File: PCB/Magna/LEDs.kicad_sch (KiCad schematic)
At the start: 94 parts, among them U2001 74HC595, U2002 74HC595, U2003 74HC595, U2004 74HC595, U2005 74HC595

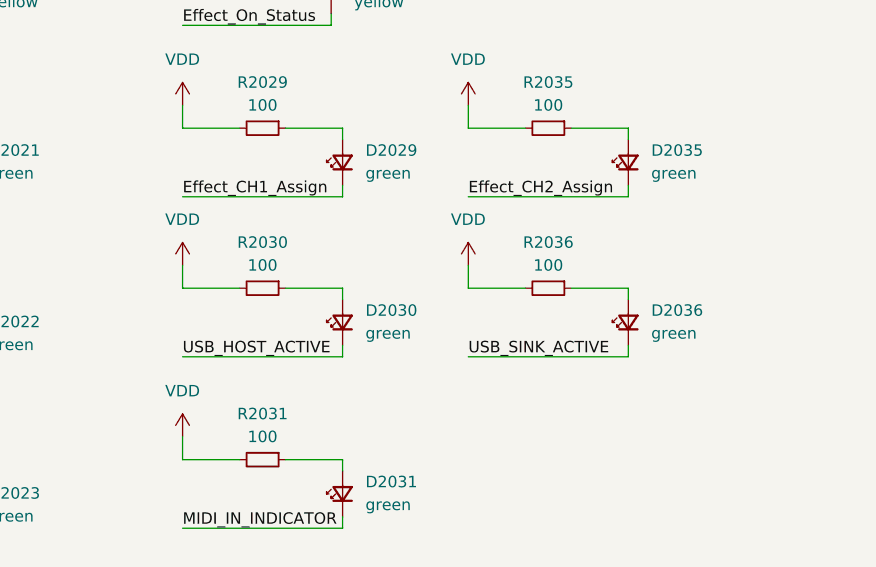
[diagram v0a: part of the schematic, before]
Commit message: Remove all ERC in schematics
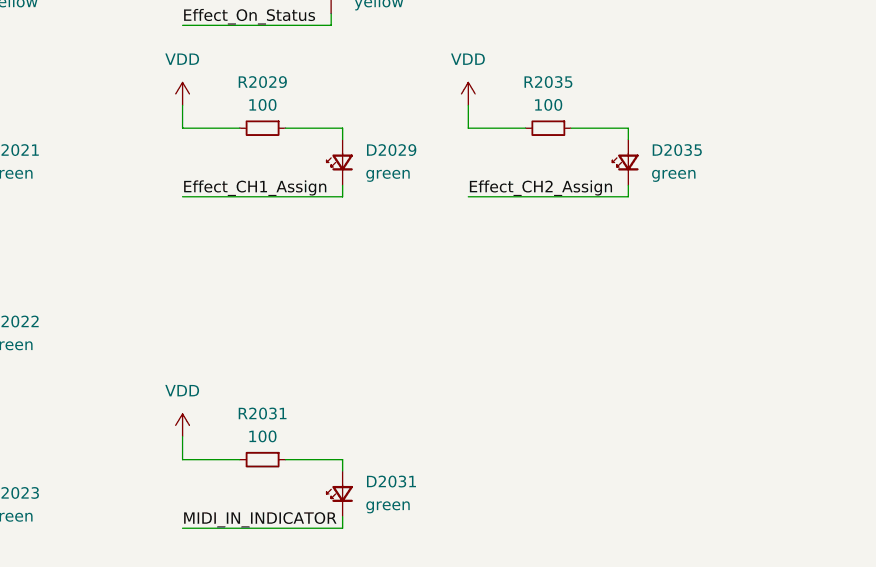
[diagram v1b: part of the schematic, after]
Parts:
- removed D2030, D2036: green, symbol Device:LED_Small
- removed R2030, R2036: 100, symbol Device:R_Small
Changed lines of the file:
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@@
     (stroke (width 0) (type default))
   )
-  (wire (pts (xy 255.27 124.46) (xy 273.05 124.46))
-    (stroke (width 0) (type default))
-  )
   (wire (pts (xy 158.75 43.18) (xy 158.75 41.91))
     (stroke (width 0) (type default))
@@
     (stroke (width 0) (type default))
   )
-  (wire (pts (xy 261.62 116.84) (xy 255.27 116.84))
-    (stroke (width 0) (type default))
-  )
   (wire (pts (xy 158.75 60.96) (xy 154.94 60.96))
     (stroke (width 0) (type default))
@@
     (stroke (width 0) (type default))
   )
-  (wire (pts (xy 241.3 123.19) (xy 241.3 124.46))
-    (stroke (width 0) (type default))
-  )
   (wire (pts (xy 99.06 176.53) (xy 73.66 176.53))
     (stroke (width 0) (type default))
@@
     (stroke (width 0) (type default))
   )
-  (wire (pts (xy 241.3 116.84) (xy 234.95 116.84))
-    (stroke (width 0) (type default))
-  )
   (wire (pts (xy 199.39 25.4) (xy 199.39 24.13))
     (stroke (width 0) (type default))
@@
     (stroke (width 0) (type default))
   )
-  (wire (pts (xy 241.3 118.11) (xy 241.3 116.84))
-    (stroke (width 0) (type default))
-  )
   (wire (pts (xy 58.42 43.18) (xy 76.2 43.18))
     (stroke (width 0) (type default))
   )
-  (wire (pts (xy 273.05 118.11) (xy 273.05 116.84))
-    (stroke (width 0) (type default))
-  )
   (wire (pts (xy 273.05 100.33) (xy 273.05 99.06))
     (stroke (width 0) (type default))
@@
     (stroke (width 0) (type default))
   )
-  (wire (pts (xy 223.52 124.46) (xy 241.3 124.46))
-    (stroke (width 0) (type default))
-  )
   (wire (pts (xy 199.39 138.43) (xy 199.39 137.16))
     (stroke (width 0) (type default))
@@
     (stroke (width 0) (type default))
   )
-  (wire (pts (xy 255.27 114.3) (xy 255.27 116.84))
-    (stroke (width 0) (type default))
-  )
   (wire (pts (xy 339.09 43.18) (xy 339.09 44.45))
     (stroke (width 0) (type default))
@@
     (stroke (width 0) (type default))
   )
-  (wire (pts (xy 223.52 114.3) (xy 223.52 116.84))
-    (stroke (width 0) (type default))
-  )
   (wire (pts (xy 158.75 80.01) (xy 154.94 80.01))
     (stroke (width 0) (type default))
@@
     (stroke (width 0) (type default))
   )
-  (wire (pts (xy 273.05 116.84) (xy 266.7 116.84))
-    (stroke (width 0) (type default))
-  )
   (wire (pts (xy 96.52 254) (xy 104.14 254))
     (stroke (width 0) (type default))
@@
     (stroke (width 0) (type default))
   )
-  (wire (pts (xy 273.05 123.19) (xy 273.05 124.46))
-    (stroke (width 0) (type default))
-  )
   (wire (pts (xy 187.96 49.53) (xy 199.39 49.53))
     (stroke (width 0) (type default))
@@
     (stroke (width 0) (type default))
   )
-  (wire (pts (xy 229.87 116.84) (xy 223.52 116.84))
-    (stroke (width 0) (type default))
-  )
   (wire (pts (xy 339.09 49.53) (xy 339.09 50.8))
     (stroke (width 0) (type default))
@@
     (effects (font (size 1.27 1.27)) (justify left bottom))
   )
-  (label "USB_SINK_ACTIVE" (at 255.27 124.46 0) (fields_autoplaced)
-    (effects (font (size 1.27 1.27)) (justify left bottom))
-  )
   (label "SPARE_LED2" (at 102.87 209.55 0) (fields_autoplaced)
     (effects (font (size 1.27 1.27)) (justify left bottom))
@@
     (effects (font (size 1.27 1.27)) (justify left bottom))
   )
-  (label "USB_HOST_ACTIVE" (at 223.52 124.46 0) (fields_autoplaced)
-    (effects (font (size 1.27 1.27)) (justify left bottom))
-  )
   (label "CH1_CUE_Status" (at 102.87 191.77 0) (fields_autoplaced)
     (effects (font (size 1.27 1.27)) (justify left bottom))
@@
     )
   )
-  (symbol (lib_id "Device:R_Small") (at 264.16 116.84 270) (unit 1)
-    (in_bom yes) (on_board yes) (dnp no) (fields_autoplaced)
-    (property "Reference" "R2036" (at 264.16 111.76 90)
-      (effects (font (size 1.27 1.27)))
-    )
-    (property "Value" "100" (at 264.16 114.3 90)
-      (effects (font (size 1.27 1.27)))
-    )
-    (property "Footprint" "" (at 264.16 116.84 0)
-      (effects (font (size 1.27 1.27)) hide)
-    )
-    (property "Datasheet" "~" (at 264.16 116.84 0)
-      (effects (font (size 1.27 1.27)) hide)
-    )
-    (pin "1")
-    (pin "2")
-    (instances
-      (project "Magna"
-        (path "/1469ea1f-a157-49dc-a369-2d42fa17695d/dad30fa9-c929-49d0-9a7d-7ccd9aecb3c4/51e532f4-93e6-4517-ac26-abaf46fe1e5c"
-          (reference "R2036") (unit 1)
-        )
-      )
-    )
-  )
   (symbol (lib_id "power:VDD") (at 147.32 96.52 0) (unit 1)
     (in_bom yes) (on_board yes) (dnp no) (fields_autoplaced)
@@
     )
   )
-  (symbol (lib_id "power:VDD") (at 255.27 114.3 0) (unit 1)
-    (in_bom yes) (on_board yes) (dnp no) (fields_autoplaced)
-    (property "Reference" "#PWR02036" (at 255.27 118.11 0)
-      (effects (font (size 1.27 1.27)) hide)
-    )
-    (property "Value" "VDD" (at 255.27 109.22 0)
-      (effects (font (size 1.27 1.27)))
-    )
-    (property "Footprint" "" (at 255.27 114.3 0)
-      (effects (font (size 1.27 1.27)) hide)
-    )
-    (property "Datasheet" "" (at 255.27 114.3 0)
-      (effects (font (size 1.27 1.27)) hide)
-    )
-    (pin "1")
-    (instances
-      (project "Magna"
-        (path "/1469ea1f-a157-49dc-a369-2d42fa17695d/dad30fa9-c929-49d0-9a7d-7ccd9aecb3c4/51e532f4-93e6-4517-ac26-abaf46fe1e5c"
-          (reference "#PWR02036") (unit 1)
-        )
-      )
-    )
-  )
   (symbol (lib_id "Device:R_Small") (at 193.04 60.96 270) (unit 1)
     (in_bom yes) (on_board yes) (dnp no) (fields_autoplaced)
@@
     )
   )
-  (symbol (lib_id "Device:LED_Small") (at 241.3 120.65 90) (unit 1)
-    (in_bom yes) (on_board yes) (dnp no) (fields_autoplaced)
-    (property "Reference" "D2030" (at 243.84 119.3165 90)
-      (effects (font (size 1.27 1.27)) (justify right))
-    )
-    (property "Value" "green" (at 243.84 121.8565 90)
-      (effects (font (size 1.27 1.27)) (justify right))
-    )
-    (property "Footprint" "" (at 241.3 120.65 90)
-      (effects (font (size 1.27 1.27)) hide)
-    )
-    (property "Datasheet" "~" (at 241.3 120.65 90)
-      (effects (font (size 1.27 1.27)) hide)
-    )
-    (pin "2")
-    (pin "1")
-    (instances
-      (project "Magna"
-        (path "/1469ea1f-a157-49dc-a369-2d42fa17695d/dad30fa9-c929-49d0-9a7d-7ccd9aecb3c4/51e532f4-93e6-4517-ac26-abaf46fe1e5c"
-          (reference "D2030") (unit 1)
-        )
-      )
-    )
-  )
   (symbol (lib_id "power:VDD") (at 187.96 58.42 0) (unit 1)
     (in_bom yes) (on_board yes) (dnp no) (fields_autoplaced)
@@
     )
   )
-  (symbol (lib_id "Device:R_Small") (at 232.41 116.84 270) (unit 1)
-    (in_bom yes) (on_board yes) (dnp no) (fields_autoplaced)
-    (property "Reference" "R2030" (at 232.41 111.76 90)
-      (effects (font (size 1.27 1.27)))
-    )
-    (property "Value" "100" (at 232.41 114.3 90)
-      (effects (font (size 1.27 1.27)))
-    )
-    (property "Footprint" "" (at 232.41 116.84 0)
-      (effects (font (size 1.27 1.27)) hide)
-    )
-    (property "Datasheet" "~" (at 232.41 116.84 0)
-      (effects (font (size 1.27 1.27)) hide)
-    )
-    (pin "1")
-    (pin "2")
-    (instances
-      (project "Magna"
-        (path "/1469ea1f-a157-49dc-a369-2d42fa17695d/dad30fa9-c929-49d0-9a7d-7ccd9aecb3c4/51e532f4-93e6-4517-ac26-abaf46fe1e5c"
-          (reference "R2030") (unit 1)
-        )
-      )
-    )
-  )
   (symbol (lib_id "power:VDD") (at 147.32 21.59 0) (unit 1)
     (in_bom yes) (on_board yes) (dnp no) (fields_autoplaced)
@@
     )
   )
-  (symbol (lib_id "power:VDD") (at 223.52 114.3 0) (unit 1)
-    (in_bom yes) (on_board yes) (dnp no) (fields_autoplaced)
-    (property "Reference" "#PWR02030" (at 223.52 118.11 0)
-      (effects (font (size 1.27 1.27)) hide)
-    )
-    (property "Value" "VDD" (at 223.52 109.22 0)
-      (effects (font (size 1.27 1.27)))
-    )
-    (property "Footprint" "" (at 223.52 114.3 0)
-      (effects (font (size 1.27 1.27)) hide)
-    )
-    (property "Datasheet" "" (at 223.52 114.3 0)
-      (effects (font (size 1.27 1.27)) hide)
-    )
-    (pin "1")
-    (instances
-      (project "Magna"
-        (path "/1469ea1f-a157-49dc-a369-2d42fa17695d/dad30fa9-c929-49d0-9a7d-7ccd9aecb3c4/51e532f4-93e6-4517-ac26-abaf46fe1e5c"
-          (reference "#PWR02030") (unit 1)
-        )
-      )
-    )
-  )
   (symbol (lib_id "power:VDD") (at 322.58 21.59 0) (unit 1)
     (in_bom yes) (on_board yes) (dnp no) (fields_autoplaced)
@@
         )
       )
-    )
-  )
-  (symbol (lib_id "Device:LED_Small") (at 273.05 120.65 90) (unit 1)
-    (in_bom yes) (on_board yes) (dnp no) (fields_autoplaced)
-    (property "Reference" "D2036" (at 275.59 119.3165 90)
-      (effects (font (size 1.27 1.27)) (justify right))
-    )
-    (property "Value" "green" (at 275.59 121.8565 90)
-      (effects (font (size 1.27 1.27)) (justify right))
-    )
-    (property "Footprint" "" (at 273.05 120.65 90)
-      (effects (font (size 1.27 1.27)) hide)
-    )
-    (property "Datasheet" "~" (at 273.05 120.65 90)
-      (effects (font (size 1.27 1.27)) hide)
-    )
-    (pin "2")
-    (pin "1")
-    (instances
-      (project "Magna"
-        (path "/1469ea1f-a157-49dc-a369-2d42fa17695d/dad30fa9-c929-49d0-9a7d-7ccd9aecb3c4/51e532f4-93e6-4517-ac26-abaf46fe1e5c"
-          (reference "D2036") (unit 1)
-        )
-      )

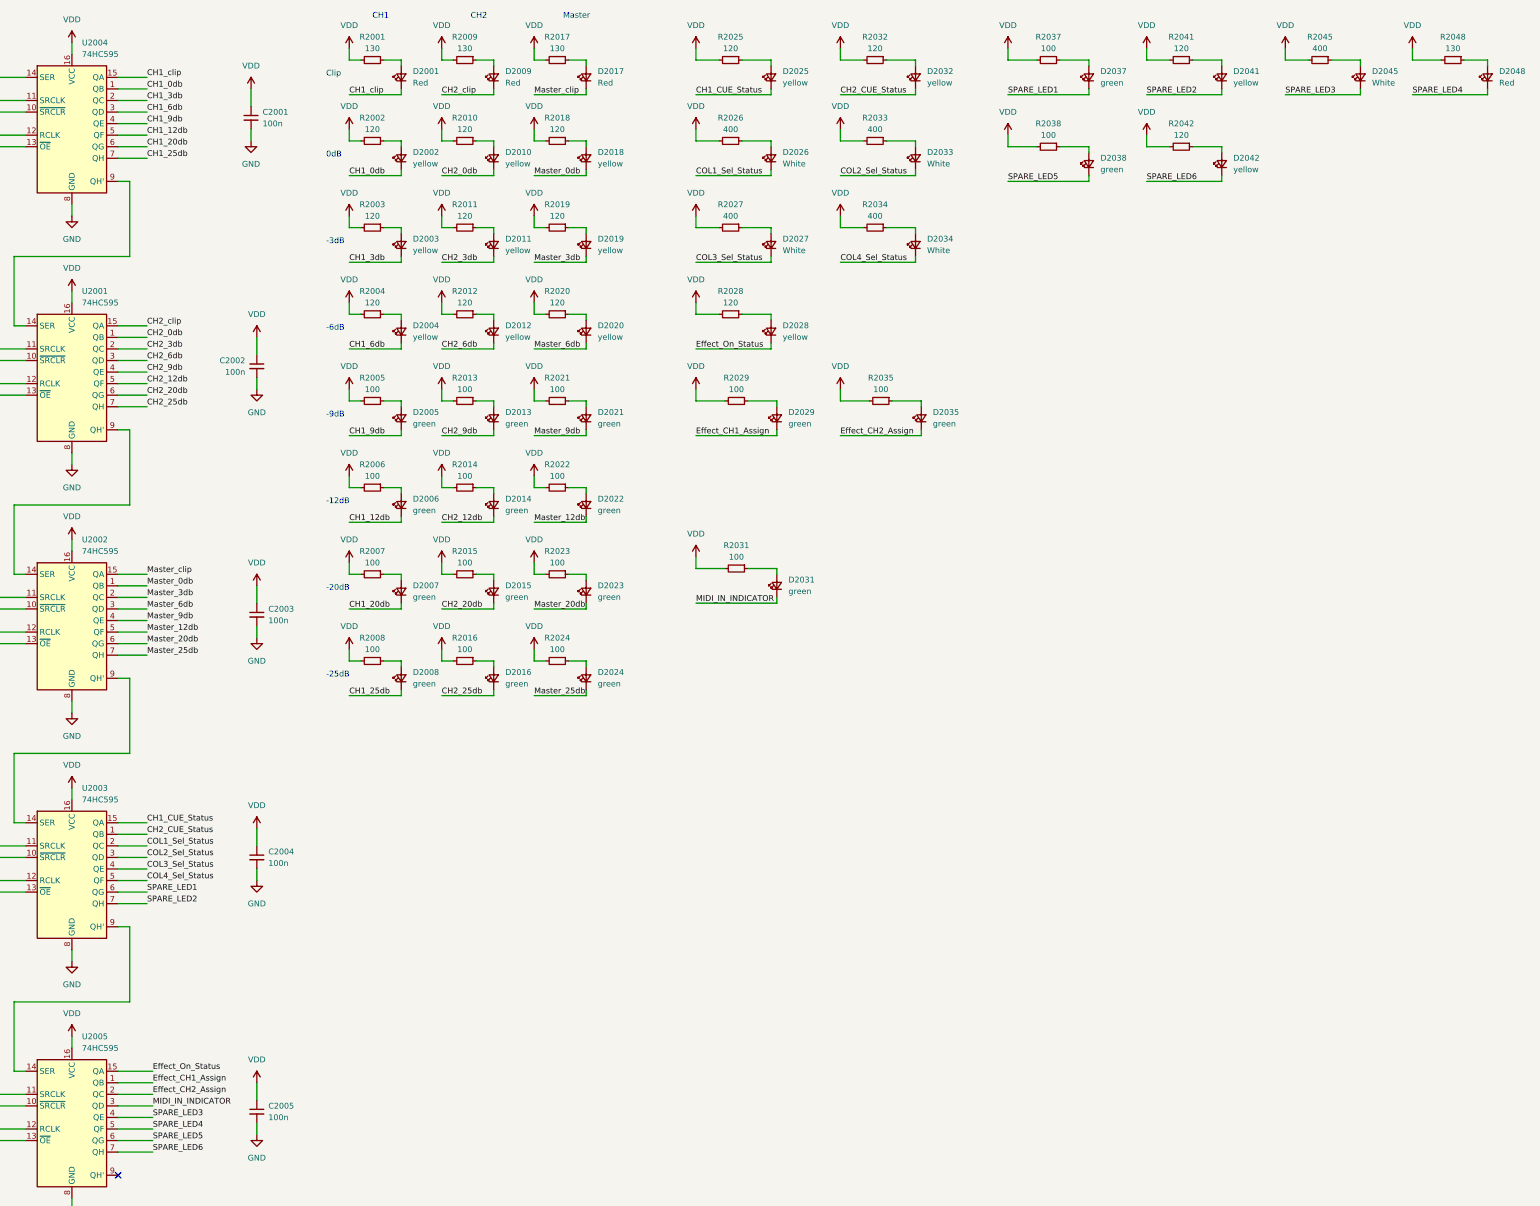
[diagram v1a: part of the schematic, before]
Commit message: Update capacitors to parts in JLC library
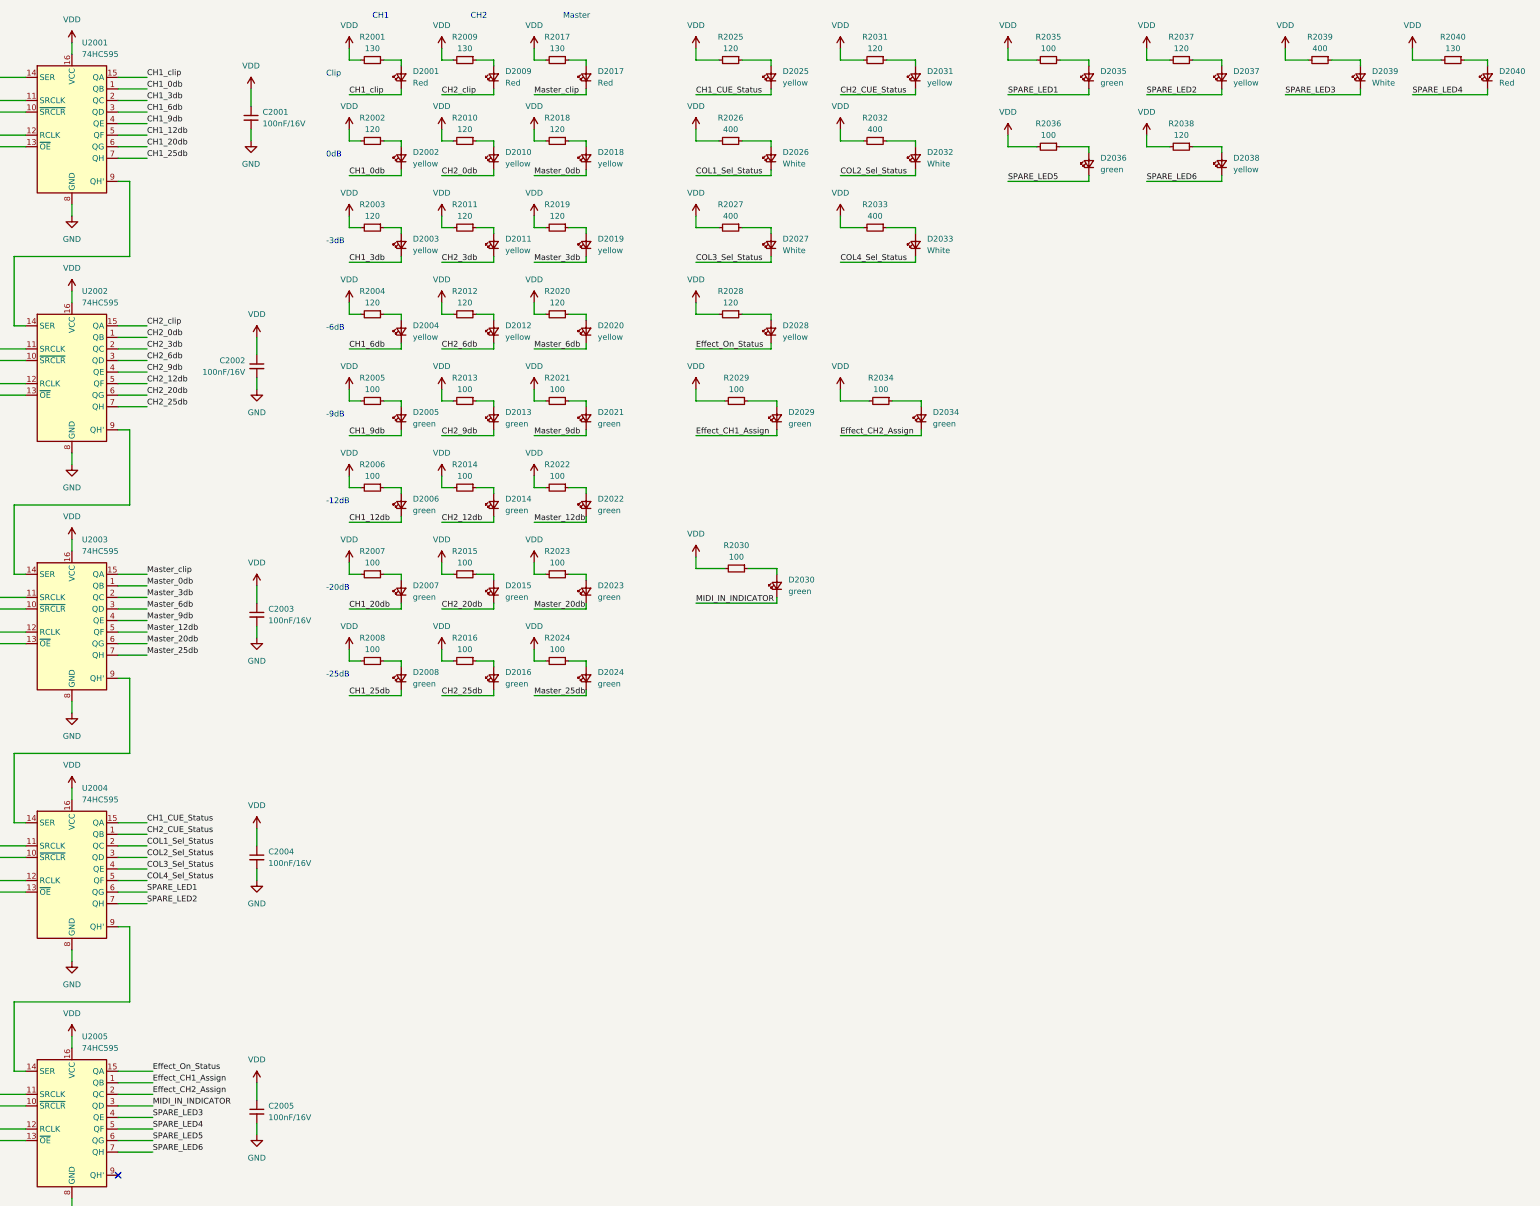
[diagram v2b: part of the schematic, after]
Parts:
- C2001, C2002, C2003, C2004, C2005: value 100n -> 100nF/16V; footprint (none) -> Capacitor_SMD:C_0805_2012Metric; LCSC (none) -> C218638
- renumbered D2031 to D2030, D2032 to D2031, D2033 to D2032, D2034 to D2033, D2035 to D2034, D2037 to D2035, D2038 to D2036, D2041 to D2037, D2042 to D2038, D2045 to D2039, D2048 to D2040, R2031 to R2030, R2032 to R2031, R2033 to R2032, R2034 to R2033, R2035 to R2034, R2037 to R2035, R2038 to R2036, R2041 to R2037, R2042 to R2038, R2045 to R2039, R2048 to R2040, U2004 to U2001, U2001 to U2002, U2002 to U2003, U2003 to U2004
